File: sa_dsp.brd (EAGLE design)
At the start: 150 x 110 mm, 416 parts, among them CN1 uSD, CN2 MINI B USB, CN3 2X5 HEADER, CN4 MINI B USB, CN5 USB A, CN6 MINI B USB, Q1 2N7002, Q2 2N7002, Q3 2N7002, Q4 2N7002, SW1 1825910-7, U1 PGA2311, U10 LME49720, U11 PGA2311, U12 LME49720, U13 LME49720, U14 PCM1754, U15 LME49720, U16 PGA2311, U17 LME49720, U18 LME49720, U19 PCM1754, U2 LM317, U20 LME49720, U21 7 SEG, U22 74HC164A, U23 PCM2707, U24 PCM2707, U25 7 SEG, U26 74HC164A, U27 LM337, U28 LM317, U29 7 SEG, U3 OSD3358-512M-BSM, U30 74HC164A, U31 100MHz, U32 USBLC6-2SC6, U33 FT230X, U34 USBLC6-2SC6, U35 USBLC6-2SC6, U36 USBLC6-2SC6, U37 2 PORT HUB, U38 TPS70925, U39 LM22670, U4 LME49720, U40 MPM3820, U41 MPM3820, U42 SN74LVC1G17D, U43 SN74LVC1G17D, U44 SN74LVC1G17D, U45 SN74LVC1G17D, U5 LME49720, U6 10CL016YF484C6G, U7 7 SEG, U8 74HC164A, U9 PCM1754

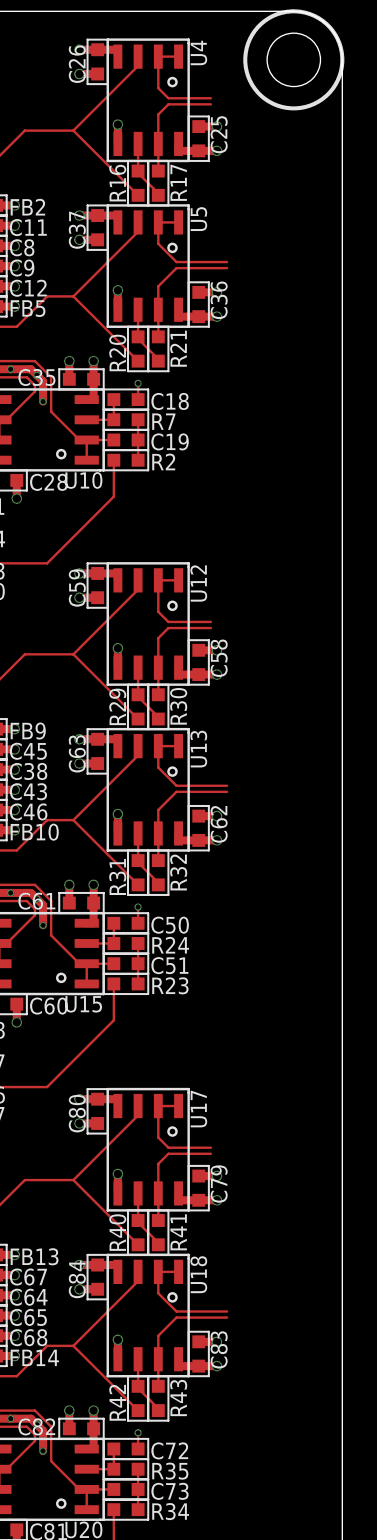
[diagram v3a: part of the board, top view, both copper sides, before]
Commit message: Analogue output connections added
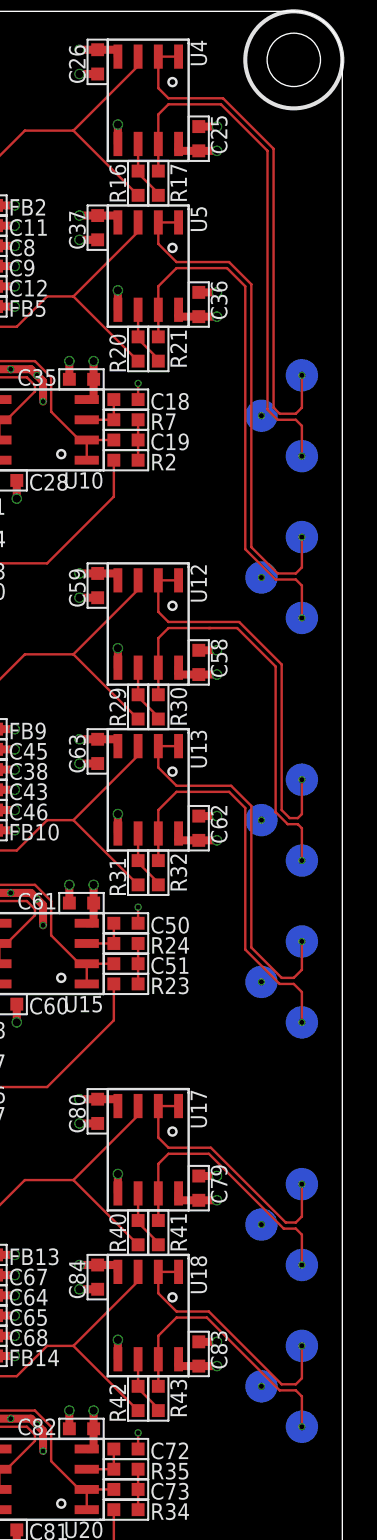
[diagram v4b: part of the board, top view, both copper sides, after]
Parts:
- added TP17, TP18, TP19, TP20, TP21, TP22, TP23, TP24, TP25, TP26, TP27, TP28, TP29, TP30, TP31, TP32, TP33, TP34: 2MM_TEST_POINT, MISC:2MM_TEST_PAD
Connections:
- net AGND: now also TP18.1, TP21.1, TP24.1, TP27.1, TP30.1, TP33.1
- net N$100: now also TP19.1
- net N$12: now also TP29.1
- net N$17: now also TP32.1
- net N$28: now also TP34.1
- net N$46: now also TP31.1
- net N$58: now also TP23.1
- net N$60: now also TP26.1
- net N$63: now also TP28.1
- net N$73: now also TP25.1
- net N$85: now also TP17.1
- net N$87: now also TP20.1
- net N$90: now also TP22.1
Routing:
- net N$12: track 7.71 -> 32.9 mm, vias 0 -> 1
- net N$46: track 7.01 -> 32.1 mm, vias 0 -> 1
- net N$28: track 7.84 -> 32.1 mm, vias 0 -> 1
- net N$17: track 7.29 -> 31.4 mm, vias 0 -> 1
- net N$73: track 7.01 -> 25.2 mm, vias 0 -> 1
- net N$58: track 7.71 -> 25.9 mm, vias 0 -> 1
- net N$63: track 7.84 -> 24.6 mm, vias 0 -> 1
- net N$60: track 7.29 -> 23.9 mm, vias 0 -> 1
- net N$85: track 7.71 -> 17.4 mm, vias 0 -> 1
- net N$100: track 7.01 -> 16.6 mm, vias 0 -> 1
- net N$87: track 7.29 -> 15.9 mm, vias 0 -> 1
- net N$90: track 7.84 -> 16.4 mm, vias 0 -> 1
- net AGND: vias 116 -> 122

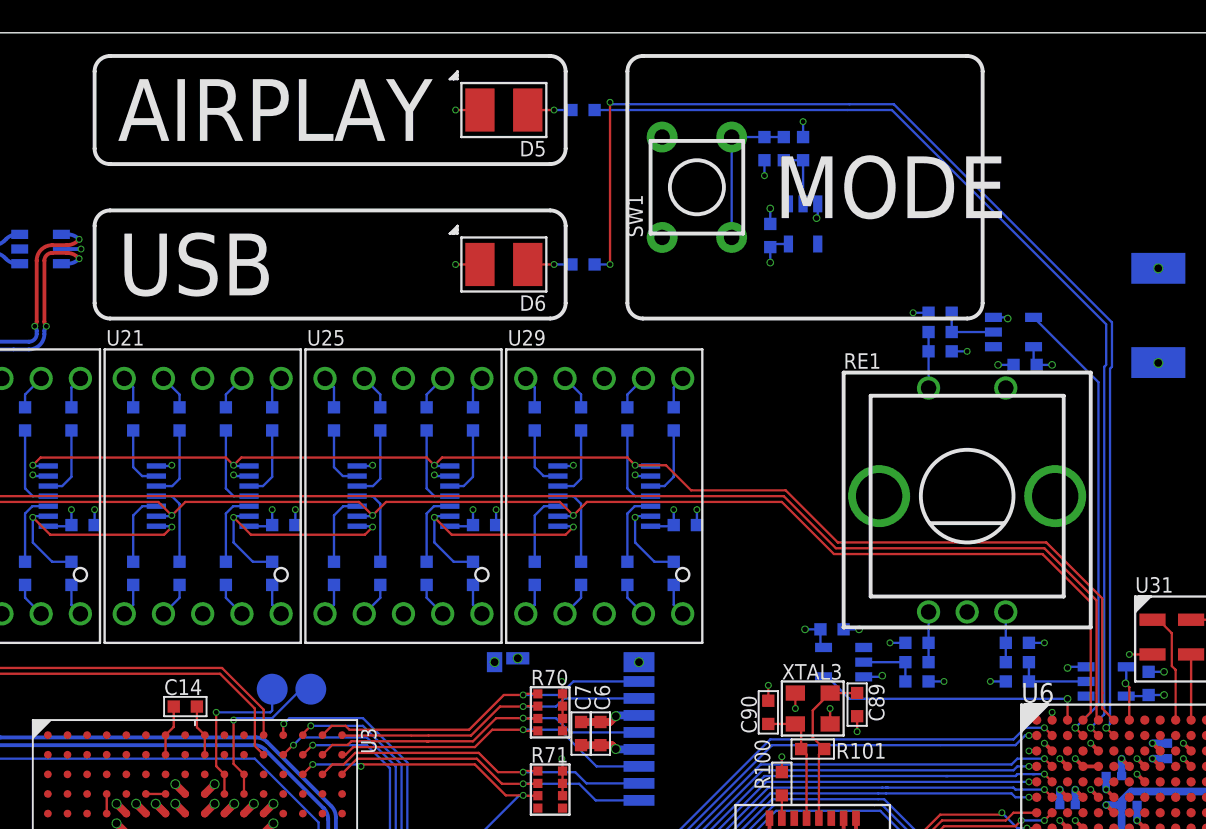
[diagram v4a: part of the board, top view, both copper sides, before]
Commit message: Connect mode button
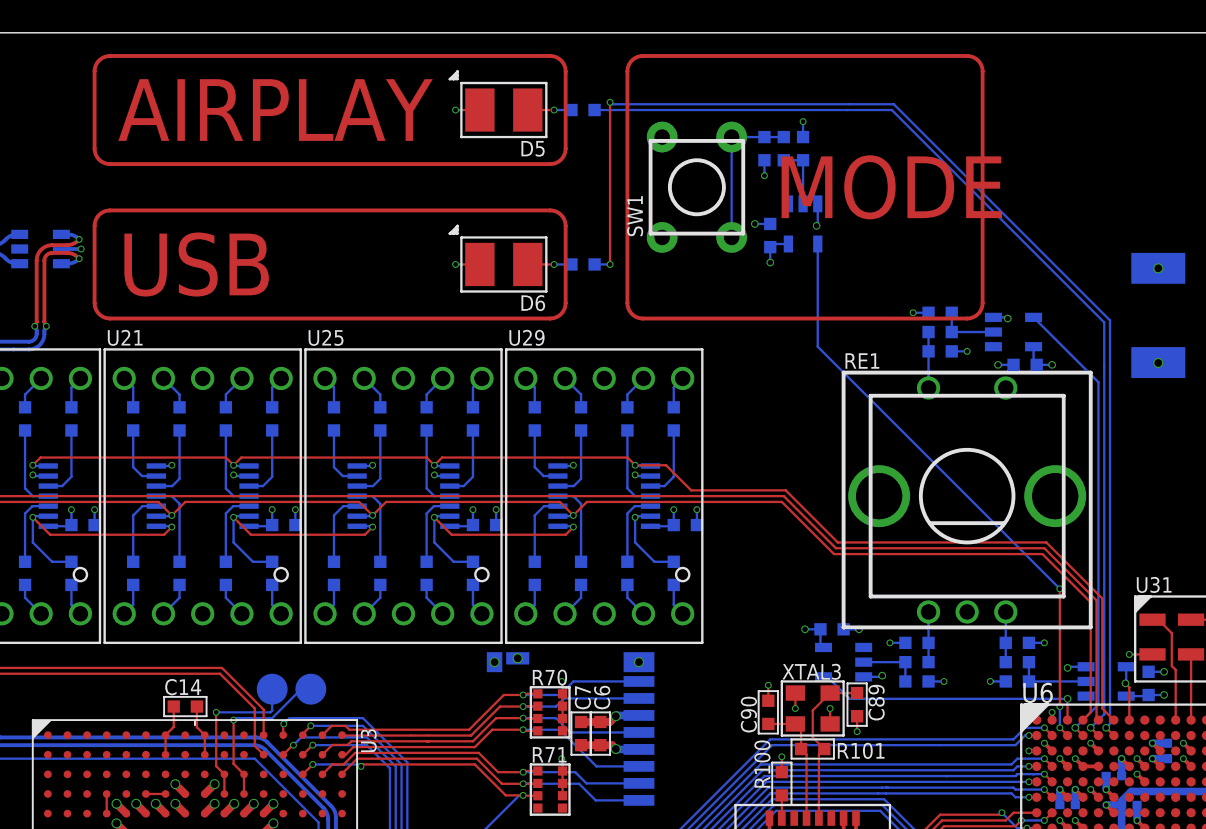
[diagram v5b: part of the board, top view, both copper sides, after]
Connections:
- net UI_INPUT_SEL: now also U6.B3
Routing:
- net UI_INPUT_SEL: track 0.00 -> 38.5 mm, vias 0 -> 3
- net N$254: track 0.00 -> 28.5 mm
- net N$251: track 0.00 -> 28.5 mm
- net N$246: track 0.00 -> 28.5 mm
- net N$242: track 0.00 -> 28.5 mm
- net N$261: track 0.00 -> 21.0 mm
- net N$258: track 0.00 -> 21.0 mm
- net N$264: track 0.00 -> 15.0 mm
- net N$260: track 0.00 -> 15.0 mm
- net N$256: track 0.00 -> 5.00 mm
- net N$252: track 0.00 -> 5.00 mm
- net N$248: track 0.00 -> 5.00 mm
- net N$244: track 0.00 -> 5.00 mm
- net N$265: track 0.00 -> 1.41 mm
- net N$263: track 0.00 -> 1.41 mm
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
